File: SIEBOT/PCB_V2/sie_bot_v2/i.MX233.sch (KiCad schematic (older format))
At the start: 90 parts, among them IC1 iMX233, J1 MICROSD, P1 CONN_12X2, P10 CONN_1, P2 CONN_12X2, P3 CONN_1, P4 CONN_4X2, P5 CONN_1, P7 CONN_1, Q1 MMDT3904, U1 ADM3101E, U3 M25P32, X1 24MHz

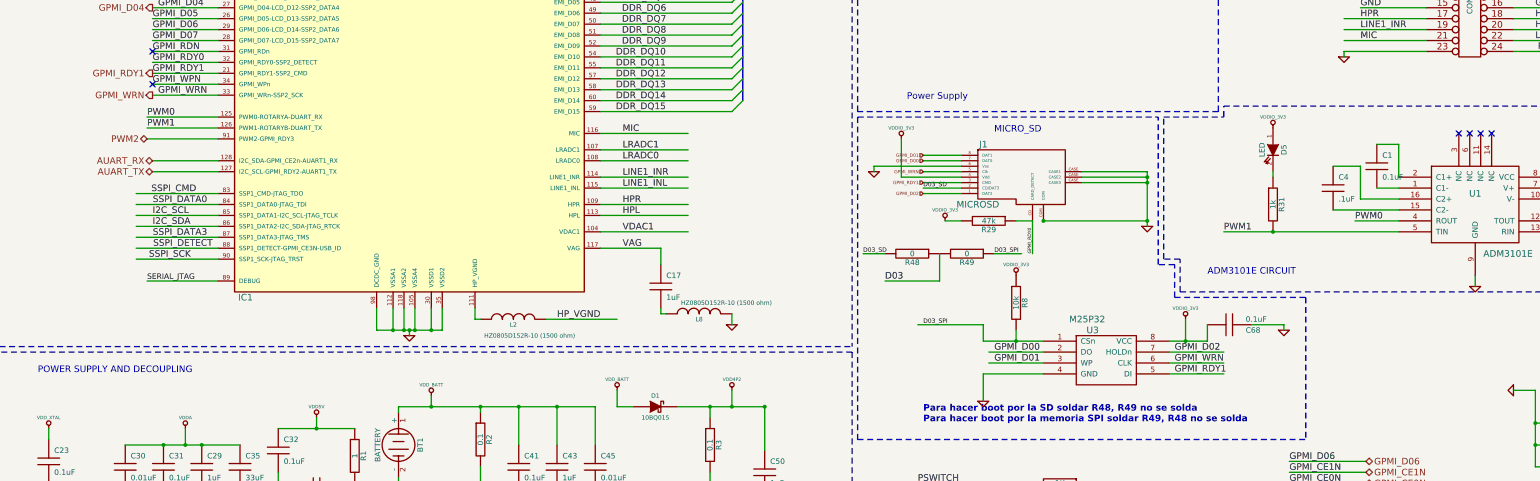
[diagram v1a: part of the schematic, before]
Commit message: Adición del Jack de alimentación, se agregó una señal BOOT_MODE para cambiar la señal BOOT0 del stm32
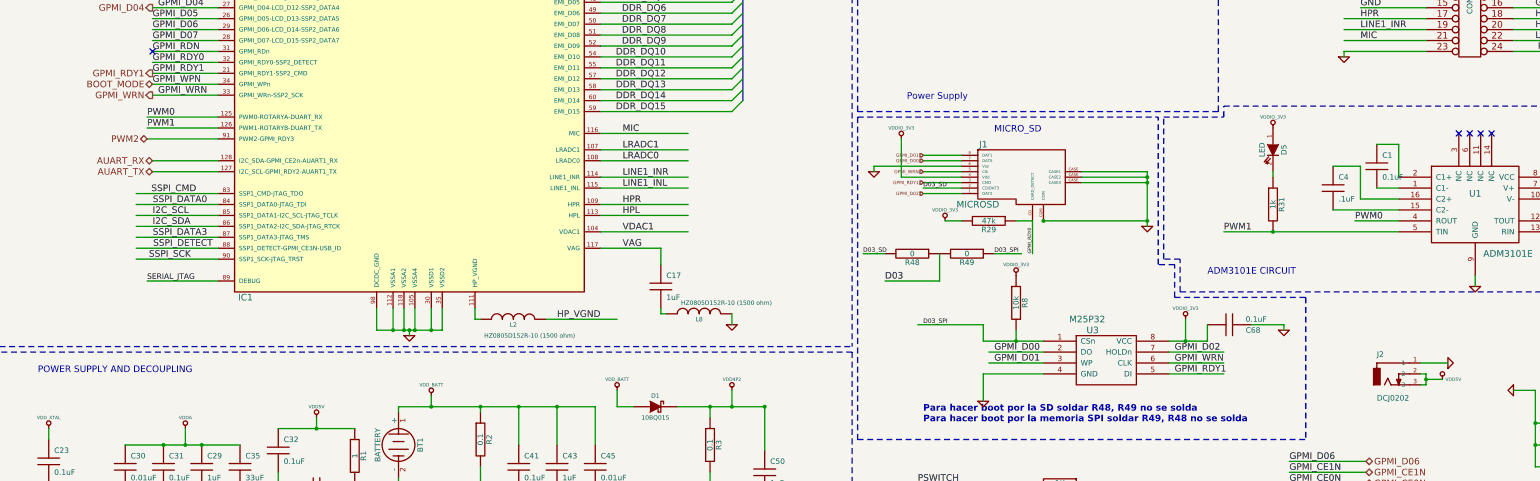
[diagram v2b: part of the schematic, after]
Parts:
- added J2: DCJ0202, DC_JACK, symbol DCJ0202
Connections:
- net labels added: BOOT_MODE
- wire segments 398 -> 403
- no-connect marks 8 -> 7

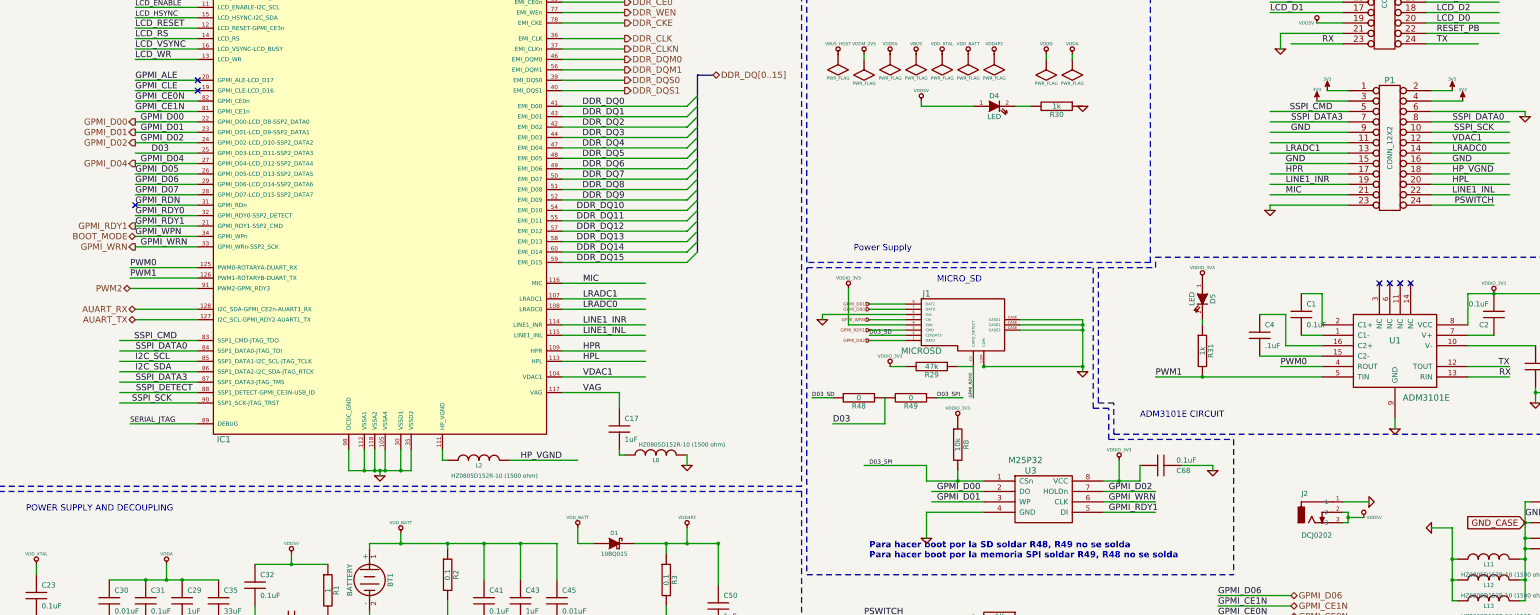
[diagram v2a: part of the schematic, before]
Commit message: USB device connector has been added
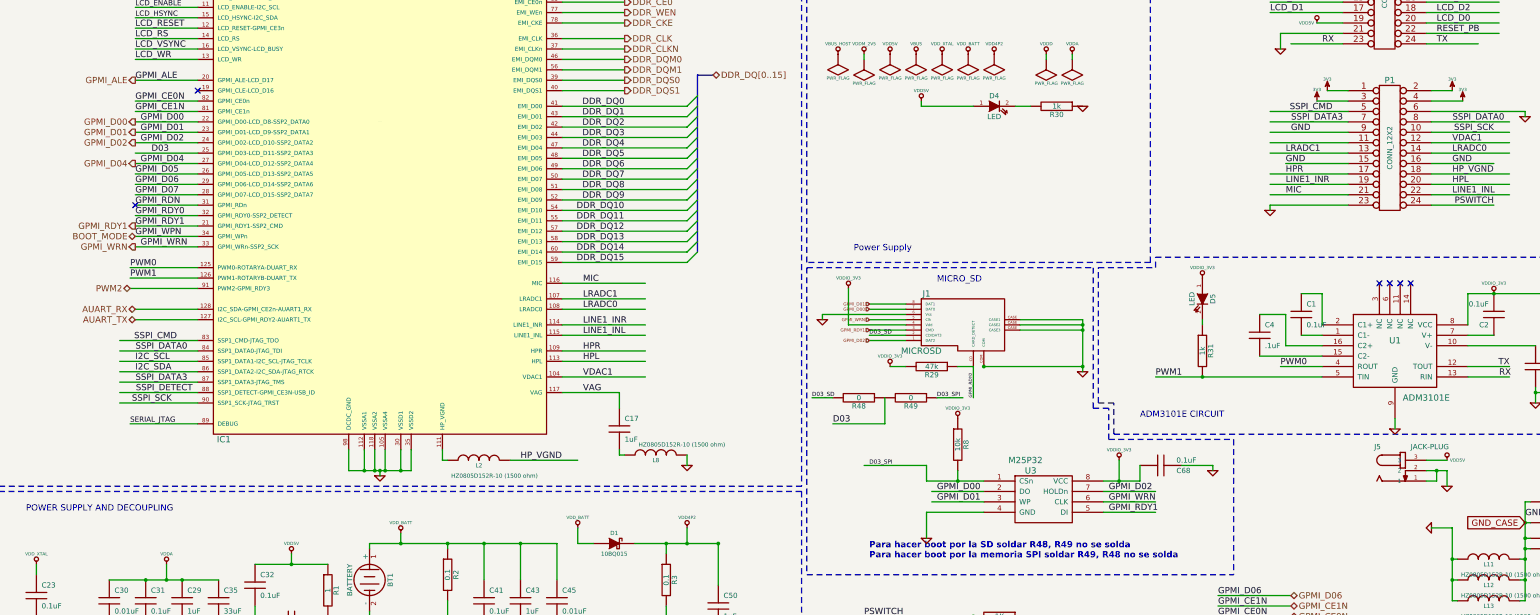
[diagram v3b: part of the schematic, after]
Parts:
- removed J2: DCJ0202, DC_JACK, symbol DCJ0202
- added J5: JACK-PLUG, DC_JACK, symbol JACK-PLUG0
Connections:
- net labels removed: GPMI_CLE
- wire segments 403 -> 402
- no-connect marks 7 -> 6
